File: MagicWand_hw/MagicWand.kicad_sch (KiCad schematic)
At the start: 90 parts, among them M1 MOTOR_NO_CONTACTS, Q7 IRLML6401, SW1 BUTTON, SW2 BUTTON, SW3 BUTTON

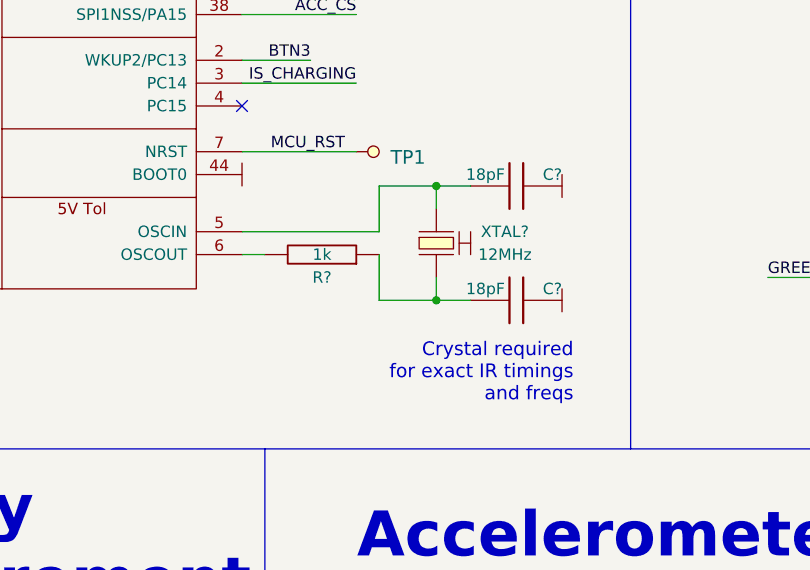
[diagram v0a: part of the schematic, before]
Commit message: Remove quartz, PCB length decreased to 99mm
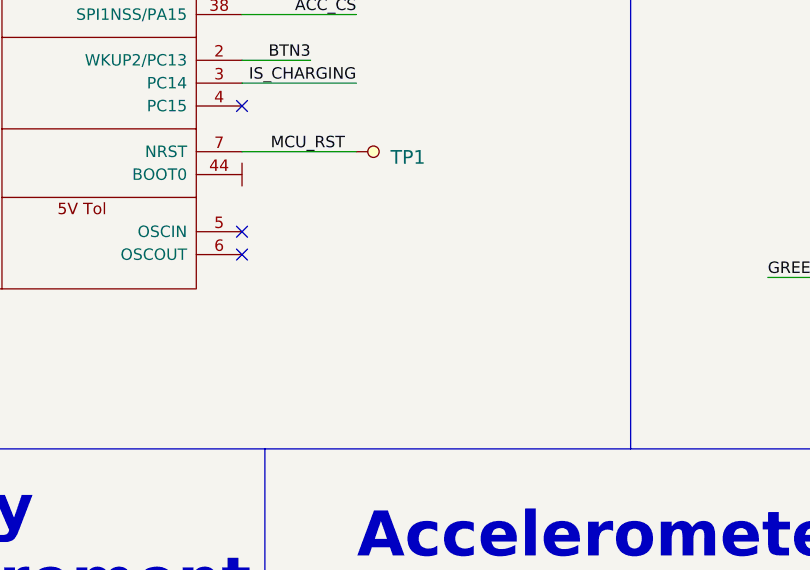
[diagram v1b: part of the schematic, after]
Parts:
- removed C? (x2): 18pF, Capacitors:CAP_0603_Silks, symbol Tittar_kl:C
- removed R?: 1k, Resistors:RES_0603_Silks, symbol Tittar_kl:R
- removed XTAL?: 12MHz, Quartz:03225C4, symbol Tittar_kl:CRYSTAL_H
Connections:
- no-connect marks 18 -> 20
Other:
- note removed: "Crystal required for exact IR timings and freqs"

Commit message: USB conn changed to real one
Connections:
- net LEDWC: now reaches R5.2, R6.2, XL5.2
- net LEDA: now reaches D2.A, D3.A, D4.A, D5.A, D?.A, XL3.1
- net LEDIRC: now reaches D?.C, XL3.2
- net LEDGC: now reaches R3.2, R4.2, XL5.1
- net LED_PWR_EN renamed PWR_EN
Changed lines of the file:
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@@
+    (effects (font (size 1.27 1.27)) (justify left bottom))
+  )
+  (label "LEDGC" (at 304.8 62.23 0) (fields_autoplaced)
     (effects (font (size 1.27 1.27)) (justify left bottom))
   )
@@
     (effects (font (size 1.27 1.27)) (justify left bottom))
   )
+  (label "LEDIRC" (at 304.8 38.1 0) (fields_autoplaced)
+    (effects (font (size 1.27 1.27)) (justify left bottom))
+  )
   (label "ACC_PWR" (at 64.77 66.04 0) (fields_autoplaced)
     (effects (font (size 1.27 1.27)) (justify left bottom))
   )
   (label "VIBRO_CTRL" (at 62.23 29.21 0) (fields_autoplaced)
+    (effects (font (size 1.27 1.27)) (justify left bottom))
+  )
+  (label "LEDA" (at 304.8 35.56 0) (fields_autoplaced)
     (effects (font (size 1.27 1.27)) (justify left bottom))
   )
@@
     (effects (font (size 1.27 1.27)) (justify right bottom))
   )
-  (label "LED_PWR_EN" (at 101.6 252.73 0) (fields_autoplaced)
+  (label "PWR_EN" (at 101.6 252.73 0) (fields_autoplaced)
     (effects (font (size 1.27 1.27)) (justify left bottom))
   )
@@
   (label "BTN3" (at 146.05 73.66 0) (fields_autoplaced)
     (effects (font (size 1.27 1.27)) (justify right bottom))
+  )
+  (label "LEDWC" (at 304.8 64.77 0) (fields_autoplaced)
+    (effects (font (size 1.27 1.27)) (justify left bottom))
   )
   (label "USB_D+" (at 73.66 156.21 0) (fields_autoplaced)
@@
     (effects (font (size 1.27 1.27)) (justify right bottom))
   )
-  (label "LED_PWR_EN" (at 63.5 35.56 0) (fields_autoplaced)
+  (label "PWR_EN" (at 63.5 35.56 0) (fields_autoplaced)
     (effects (font (size 1.27 1.27)) (justify left bottom))
   )

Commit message: + Full hex added
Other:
- note added: "Replace R25 to 15k, R28 to 5k1"
- note added: "Replace R3 & R4 to 0R"
- note added: "Replace R5 & R6 to 5R1"
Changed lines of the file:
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@@
     (stroke (width 0) (type default))
+  )
+  (text "Replace R5 & R6 to 5R1" (at 360.68 67.31 0)
+    (effects (font (size 1.27 1.27)) (justify left bottom))
   )
   (text "Power" (at 170.18 208.28 0)
@@
     (effects (font (size 1.524 1.524)) (justify left bottom))
   )
+  (text "Replace R3 & R4 to 0R" (at 334.01 67.31 0)
+    (effects (font (size 1.27 1.27)) (justify left bottom))
+  )
   (text "IR Transmitter & LEDs" (at 278.13 25.4 0)
     (effects (font (size 5 5) (thickness 1) bold) (justify right bottom))
@@
     (effects (font (size 5 5) (thickness 1) bold) (justify right bottom))
   )
+  (text "Replace R25 to 15k, R28 to 5k1" (at 168.91 260.35 0)
+    (effects (font (size 1.27 1.27)) (justify left bottom))
+  )
   (text "Battery connector" (at 15.24 232.41 0)
